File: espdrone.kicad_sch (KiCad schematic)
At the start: 56 parts, among them J1 Conn_02x03_Odd_Even, J12 Conn_01x14, J2 Conn_01x02, U2 USBLC6-2P6, U3 W25Q128JVP, Y1 Crystal_GND24

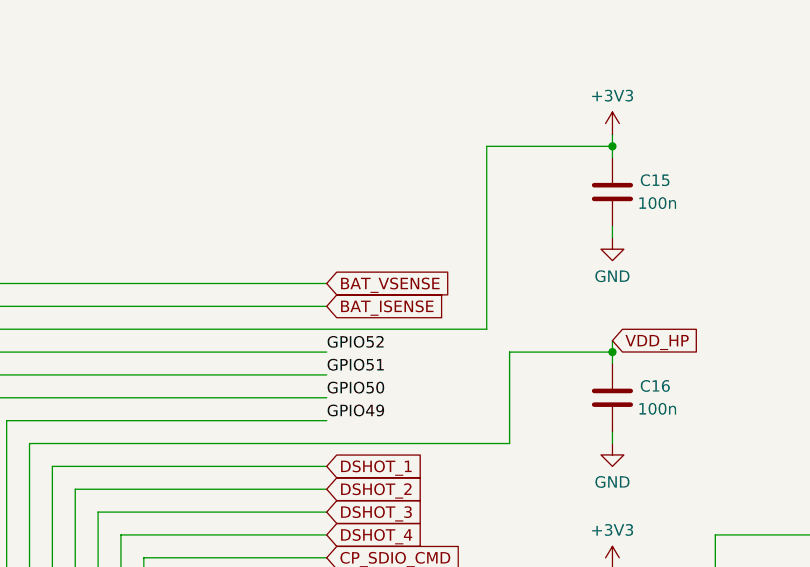
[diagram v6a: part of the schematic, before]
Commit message: Update PCB stackup and design rules
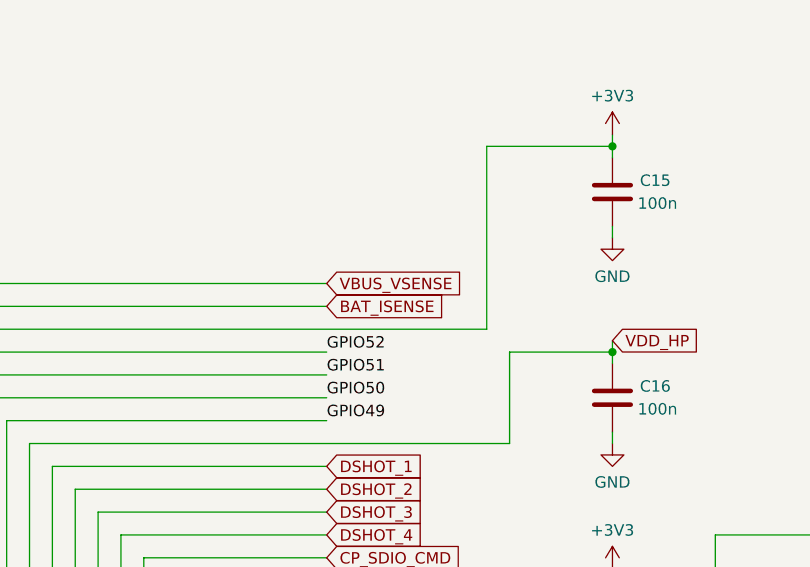
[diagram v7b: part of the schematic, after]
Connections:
- net BAT_VSENSE renamed VBUS_VSENSE
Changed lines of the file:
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@@
 		)
 	)
-	(global_label "BAT_VSENSE"
+	(global_label "VBUS_VSENSE"
 		(shape input)
 		(at 173.99 82.55 0)
@@
 		)
 		(property "Intersheetrefs" "${INTERSHEET_REFS}"
-			(at 188.4051 82.55 0)
+			(at 189.9775 82.55 0)
 			(hide yes)
 			(show_name no)

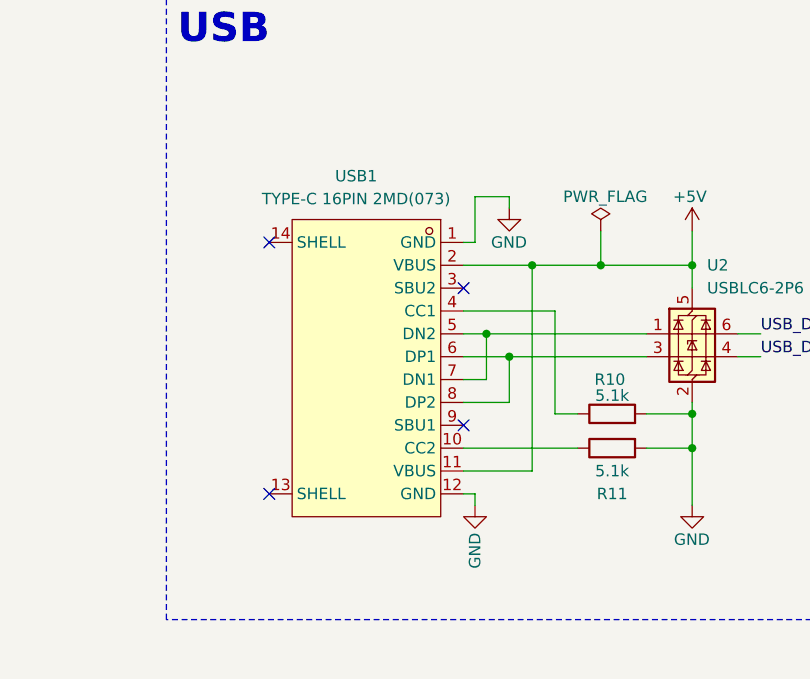
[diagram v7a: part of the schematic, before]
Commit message: Fix USB-C connector footprint
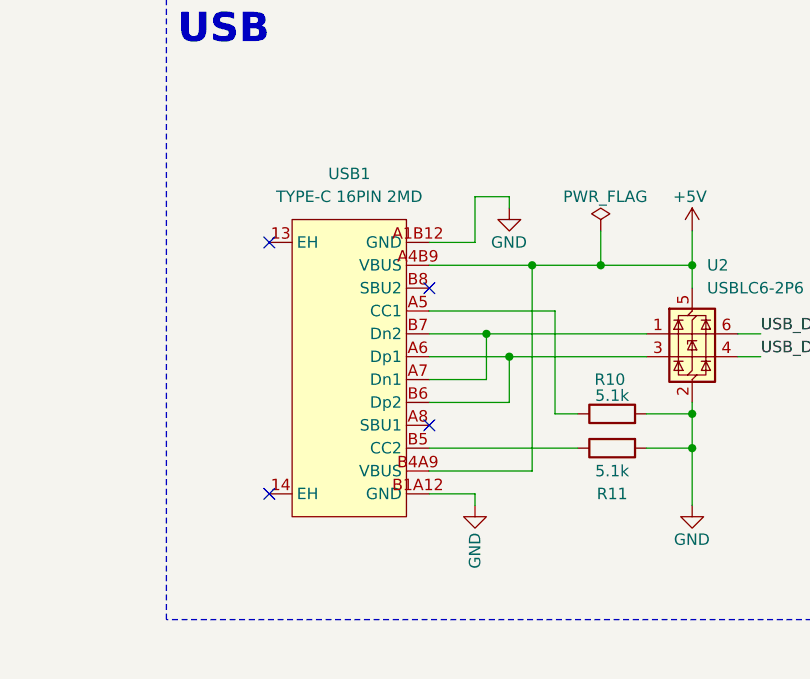
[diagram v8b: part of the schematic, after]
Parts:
- removed USB1: TYPE-C 16PIN 2MD(073), easyeda2kicad:USB-C-SMD_TYPE-C-16PIN-2MD-073, symbol easyeda2kicad:TYPE-C16PIN2MD(073)
- added USB1: TYPE-C 16PIN 2MD, easyeda2kicad:USB-C-SMD_TYPE-C-16PIN-2MD-073, symbol easyeda2kicad:TYPE-C16PIN2MD
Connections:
- net +5V: now also USB1.A4B9 (VBUS), USB1.B4A9 (VBUS)
- net GND: now also USB1.A1B12 (GND), USB1.B1A12 (GND)
- net at R10.1: now also USB1.A5 (CC1)
- net at R11.1: now also USB1.B5 (CC2)
- net at U2.1 (I/O1): now also USB1.A7 (Dn1), USB1.B7 (Dn2)
- net at U2.3 (I/O2): now also USB1.A6 (Dp1), USB1.B6 (Dp2)
